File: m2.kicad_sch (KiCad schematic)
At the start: 59 parts, among them J13 Bus_M.2_1-2199230-6, J14 Bus_M.2_2199230-2, Y3 Oscillator_32.768kHz_ECS_2520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

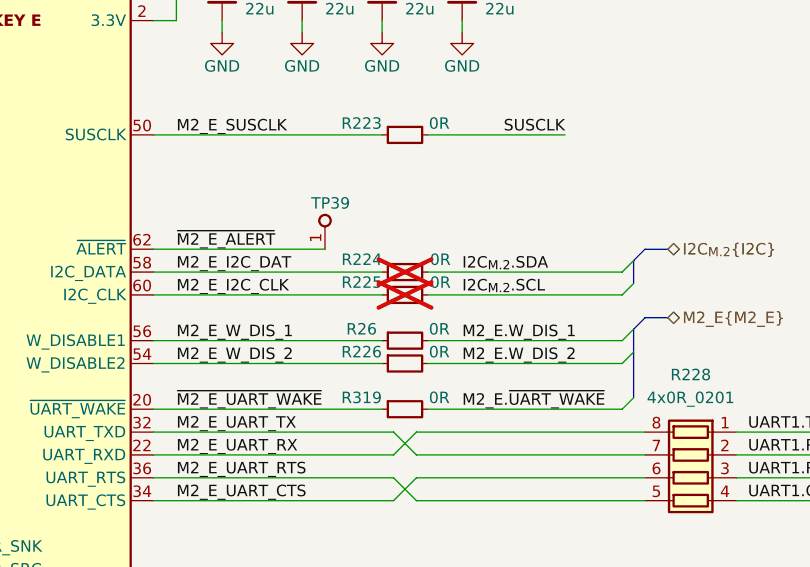
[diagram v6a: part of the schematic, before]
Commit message: [#84355] Add antmicro logo to PCB
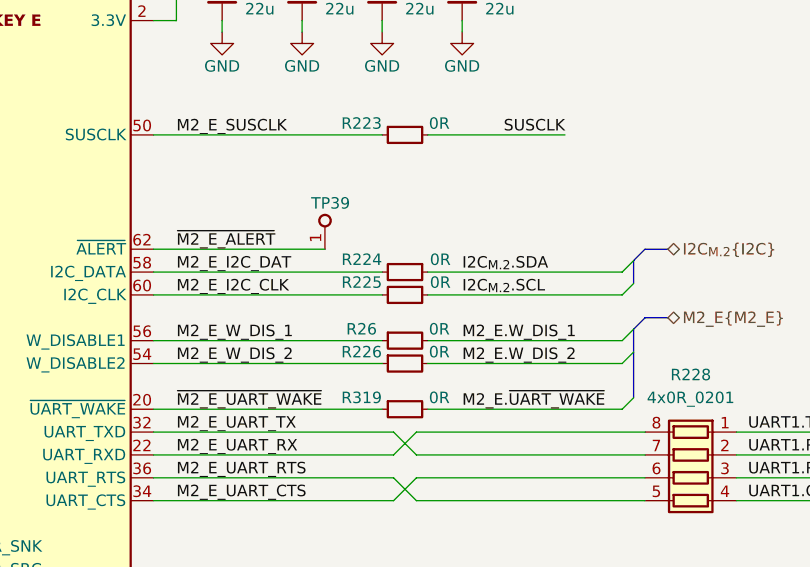
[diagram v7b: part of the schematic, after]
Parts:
- R224, R225: now fitted; now in the parts list
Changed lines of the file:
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@@
 		(unit 1)
 		(exclude_from_sim no)
-		(in_bom no)
+		(in_bom yes)
 		(on_board yes)
-		(dnp yes)
+		(dnp no)
 		(property "Reference" "R224"
 			(at 318.77 121.285 0)
@@
 		(unit 1)
 		(exclude_from_sim no)
-		(in_bom no)
+		(in_bom yes)
 		(on_board yes)
-		(dnp yes)
+		(dnp no)
 		(property "Reference" "R225"
 			(at 318.77 123.825 0)

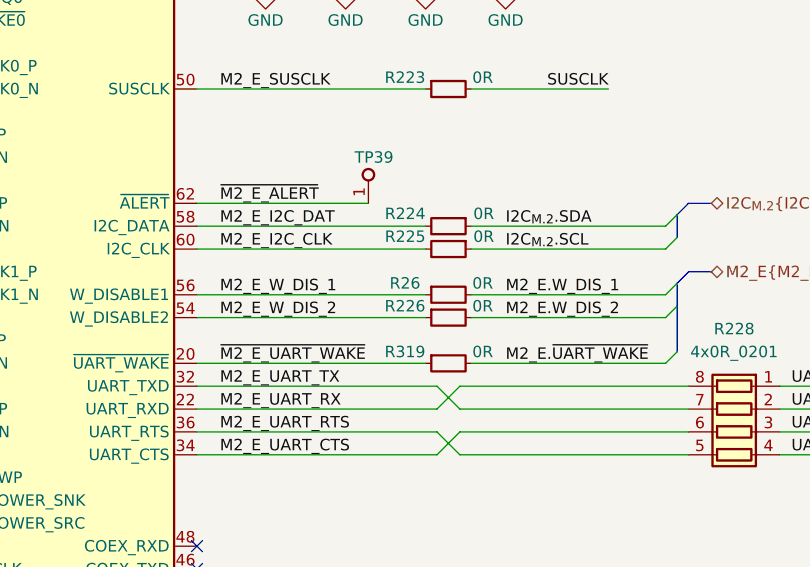
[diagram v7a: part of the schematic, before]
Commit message: [#84355] WIP: Route single ended M.2 key E signals
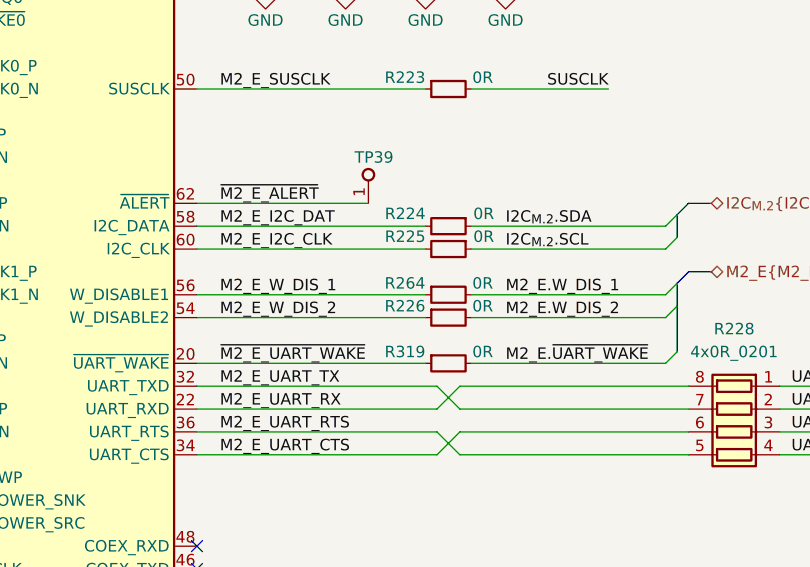
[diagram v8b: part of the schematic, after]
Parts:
- removed R26: R_0R_0402, antmicro-footprints:R_0402_1005Metric, symbol antmicroResistors0402:R_0R_0402
- added R264: R_0R_0402, antmicro-footprints:R_0402_1005Metric, symbol antmicroResistors0402:R_0R_0402
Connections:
- net M2_E.W_DIS_1: now also R264.2
- net M2_E_W_DIS_1: now also R264.1
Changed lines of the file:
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@@
-	)
-	(symbol
-		(lib_id "antmicroResistors0402:R_0R_0402")
-		(at 318.77 129.54 0)
-		(unit 1)
-		(exclude_from_sim no)
-		(in_bom yes)
-		(on_board yes)
-		(dnp no)
-		(property "Reference" "R26"
-			(at 316.484 128.27 0)
-			(effects
-				(font
-					(size 1.27 1.27)
-					(thickness 0.15)
-				)
-			)
-		)
-		(property "Value" "R_0R_0402"
-			(at 339.09 142.24 0)
-			(effects
-				(font
-					(size 1.27 1.27)
-					(thickness 0.15)
-				)
-				(justify left bottom)
-				(hide yes)
-			)
-		)
-		(property "Footprint" "antmicro-footprints:R_0402_1005Metric"
-			(at 339.09 144.78 0)
-			(effects
-				(font
-					(size 1.27 1.27)
-					(thickness 0.15)
-				)
-				(justify left bottom)
-				(hide yes)
-			)
-		)
-		(property "Datasheet" "https://industrial.panasonic.com/cdbs/www-data/pdf/RDA0000/AOA0000C301.pdf"
-			(at 339.09 147.32 0)
-			(effects
-				(font
-					(size 1.27 1.27)
-					(thickness 0.15)
-				)
-				(justify left bottom)
-				(hide yes)
-			)
-		)
-		(property "Description" "SMD Chip Resistor, Jumper, 0 ohm, 100 mW, 0402 [1005 Metric], Thick Film, General Purpose"
-			(at 318.77 129.54 0)
-			(effects
-				(font
-					(size 1.27 1.27)
-				)
-				(hide yes)
-			)
-		)
-		(property "MPN" "ERJ2GE0R00X"
-			(at 339.09 149.86 0)
-			(effects
-				(font
-					(size 1.27 1.27)
-					(thickness 0.15)
-				)
-				(justify left bottom)
-				(hide yes)
-			)
-		)
-		(property "Manufacturer" "Panasonic"
-			(at 339.09 152.4 0)
-			(effects
-				(font
-					(size 1.27 1.27)
-					(thickness 0.15)
-				)
-				(justify left bottom)
-				(hide yes)
-			)
-		)
-		(property "License" "Apache-2.0"
-			(at 339.09 154.94 0)
-			(effects
-				(font
-					(size 1.27 1.27)
-					(thickness 0.15)
-				)
-				(justify left bottom)
-				(hide yes)
-			)
-		)
-		(property "Val" "0R"
-			(at 325.12 128.27 0)
-			(effects
-				(font
-					(size 1.27 1.27)
-					(thickness 0.15)
-				)
-			)
-		)
-		(property "Tolerance" "~"
-			(at 339.09 139.7 0)
-			(effects
-				(font
-					(size 1.27 1.27)
-				)
-				(justify left bottom)
-				(hide yes)
-			)
-		)
-		(property "Current" "1A"
-			(at 321.31 125.73 0)
-			(effects
-				(font
-					(size 1.27 1.27)
-					(thickness 0.15)
-				)
-				(hide yes)
-			)
-		)
-		(property "Author" "Antmicro"
-			(at 339.09 157.48 0)
-			(effects
-				(font
-					(size 1.27 1.27)
-					(thickness 0.15)
-				)
-				(justify left bottom)
-				(hide yes)
-			)
-		)
-		(property "Public" "False"
-			(at 339.09 160.02 0)
-			(effects
-				(font
-					(size 1.27 1.27)
-				)
-				(justify left bottom)
-				(hide yes)
-			)
-		)
-		(pin "1"
-		)
-		(pin "2"
-		)
-		(instances
-			(project "jetson-agx-thor-baseboard"
-				(path "/f569b0be-0afd-48b7-93ee-28582a4c645c/456a2f48-4934-4d0e-aaf0-f39b01ccc0c1"
-					(reference "R26")
-					(unit 1)
-				)
-			)
-		)
 	)
 	(symbol
@@
 					(unit 1)
 				)
+			)
+		)
+	)
+	(symbol
+		(lib_id "antmicroResistors0402:R_0R_0402")
+		(at 318.77 129.54 0)
+		(unit 1)
+		(exclude_from_sim no)
+		(in_bom yes)
+		(on_board yes)
+		(dnp no)
+		(property "Reference" "R264"
+			(at 316.484 128.27 0)
+			(effects
+				(font
+					(size 1.27 1.27)
+					(thickness 0.15)
+				)
+			)
+		)
+		(property "Value" "R_0R_0402"
+			(at 339.09 142.24 0)
+			(effects
+				(font
+					(size 1.27 1.27)
+					(thickness 0.15)
+				)
+				(justify left bottom)
+				(hide yes)
+			)
+		)
+		(property "Footprint" "antmicro-footprints:R_0402_1005Metric"
+			(at 339.09 144.78 0)
+			(effects
+				(font
+					(size 1.27 1.27)
+					(thickness 0.15)
+				)
+				(justify left bottom)
+				(hide yes)
+			)
+		)
+		(property "Datasheet" "https://industrial.panasonic.com/cdbs/www-data/pdf/RDA0000/AOA0000C301.pdf"
+			(at 339.09 147.32 0)
+			(effects
+				(font
+					(size 1.27 1.27)
+					(thickness 0.15)
+				)
+				(justify left bottom)
+				(hide yes)
+			)
+		)
+		(property "Description" "SMD Chip Resistor, Jumper, 0 ohm, 100 mW, 0402 [1005 Metric], Thick Film, General Purpose"
+			(at 318.77 129.54 0)
+			(effects
+				(font
+					(size 1.27 1.27)
+				)
+				(hide yes)
+			)
+		)
+		(property "MPN" "ERJ2GE0R00X"
+			(at 339.09 149.86 0)
+			(effects
+				(font
+					(size 1.27 1.27)
+					(thickness 0.15)
+				)
+				(justify left bottom)
+				(hide yes)
+			)
+		)
+		(property "Manufacturer" "Panasonic"
+			(at 339.09 152.4 0)
+			(effects
+				(font
+					(size 1.27 1.27)
+					(thickness 0.15)
+				)
+				(justify left bottom)
+				(hide yes)
+			)
+		)
+		(property "License" "Apache-2.0"
+			(at 339.09 154.94 0)
+			(effects
+				(font
+					(size 1.27 1.27)
+					(thickness 0.15)
+				)
+				(justify left bottom)
+				(hide yes)
+			)
+		)
+		(property "Val" "0R"
+			(at 325.12 128.27 0)
+			(effects
+				(font
+					(size 1.27 1.27)
+					(thickness 0.15)
+				)
+			)
+		)
+		(property "Tolerance" "~"
+			(at 339.09 139.7 0)
+			(effects
+				(font
+					(size 1.27 1.27)
+				)
+				(justify left bottom)
+				(hide yes)
+			)
+		)
+		(property "Current" "1A"
+			(at 321.31 125.73 0)
+			(effects
+				(font
+					(size 1.27 1.27)
+					(thickness 0.15)
+				)
+				(hide yes)
+			)
+		)
+		(property "Author" "Antmicro"
+			(at 339.09 157.48 0)
+			(effects
+				(font
+					(size 1.27 1.27)
+					(thickness 0.15)
+				)
+				(justify left bottom)
+				(hide yes)
+			)
+		)
+		(property "Public" "False"
+			(at 339.09 160.02 0)
+			(effects
+				(font
+					(size 1.27 1.27)
+				)
+				(justify left bottom)
+				(hide yes)
+			)
+		)
+		(pin "1"
+		)
+		(pin "2"
+		)
+		(instances
+			(project "jetson-agx-thor-baseboard"
+				(path "/f569b0be-0afd-48b7-93ee-28582a4c645c/456a2f48-4934-4d0e-aaf0-f39b01ccc0c1"
+					(reference "R264")
+					(unit 1)
+				)
